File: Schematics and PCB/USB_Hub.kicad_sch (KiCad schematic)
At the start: 95 parts, among them J6 UPSTREAM, J7 DOWNSTREAM_3, J8 DOWNSTREAM_1, J9 DOWNSTREAM_2, U16 TUSB8042A, U17 TPS2561, U18 TLV71311PDBVR, U19 TLV70033DDCR, U20 TPS2561, Y1 24MHz 20pF GND24

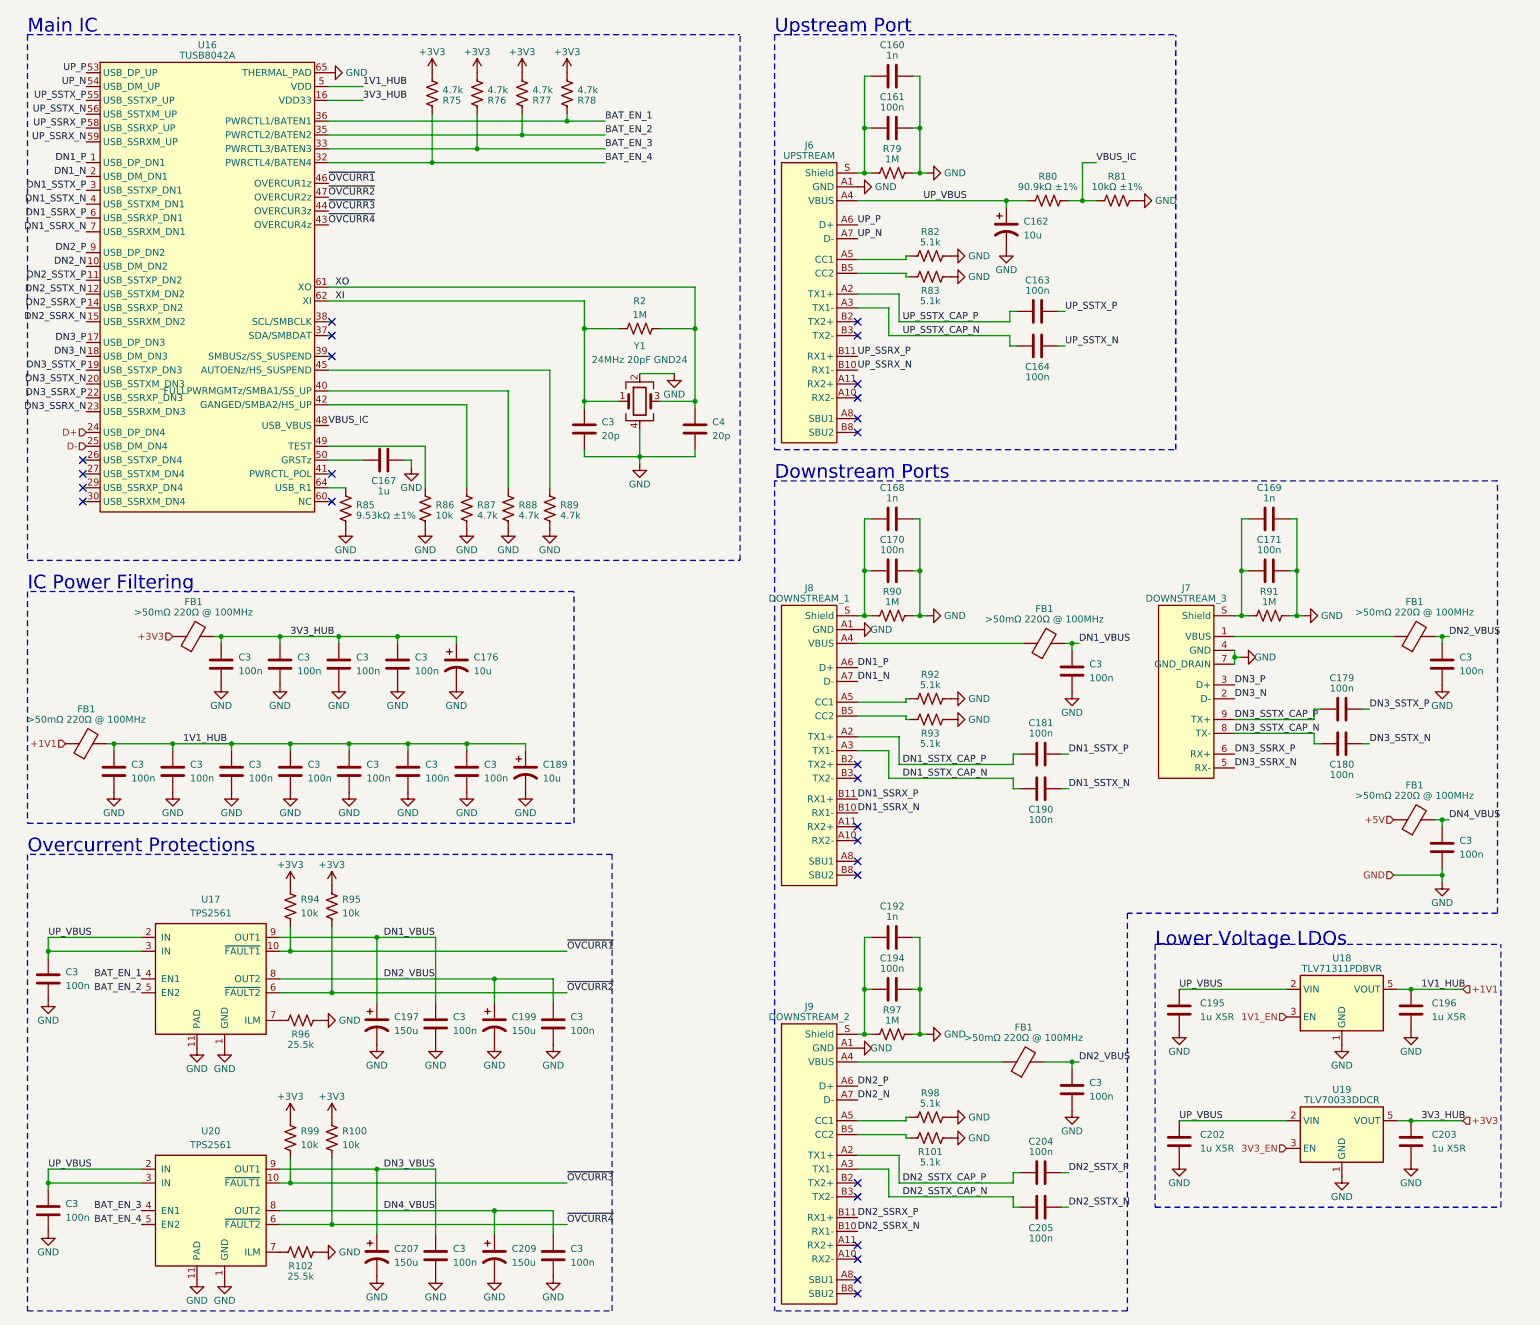
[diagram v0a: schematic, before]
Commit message: route most of the differential pairs
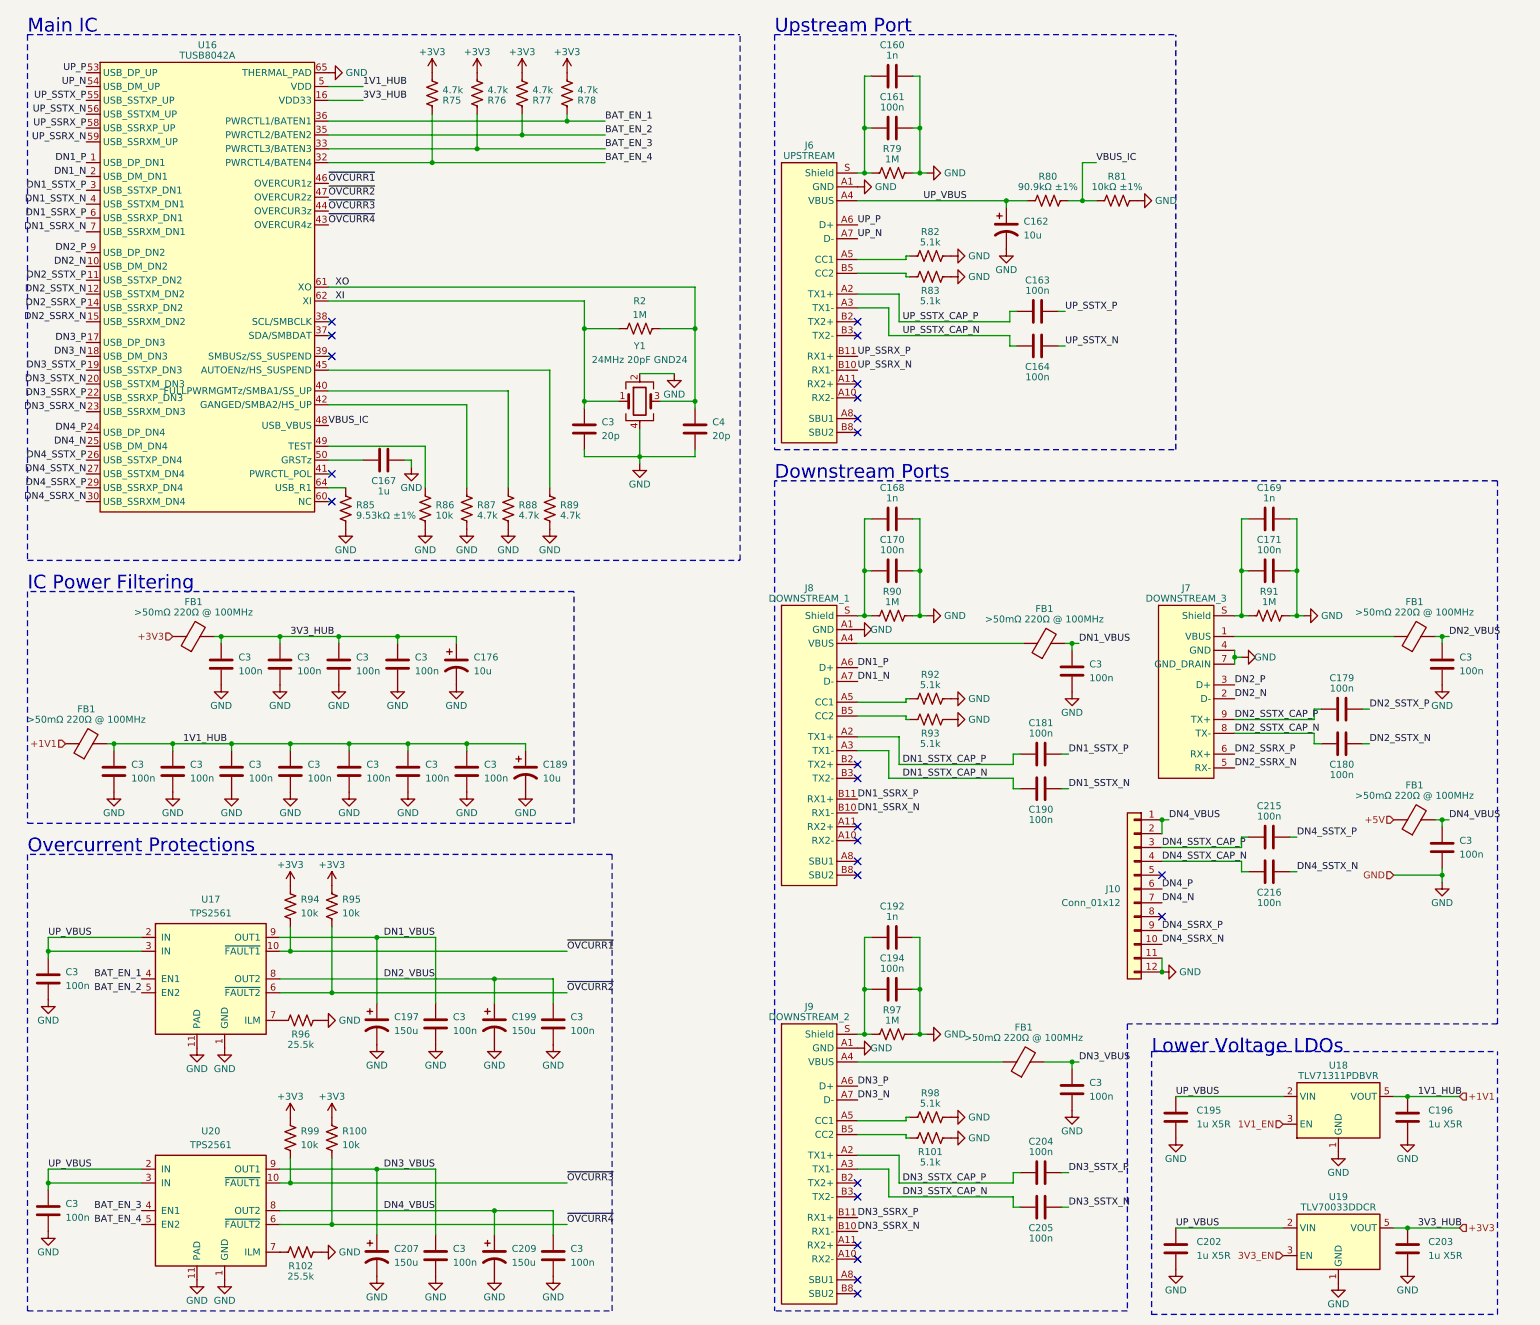
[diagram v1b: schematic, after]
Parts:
- added C215, C216: 100n, Capacitor_SMD:C_0603_1608Metric, symbol Device:C
- added J10: Conn_01x12, Connector_FFC-FPC:Hirose_FH12-12S-0.5SH_1x12-1MP_P0.50mm_Horizontal, symbol Connector_Generic:Conn_01x12
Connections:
- net DN2_N: now also J7.2 (D-); no longer J9.A7 (D-), J9.B7 (D-)
- net DN2_P: now also J7.3 (D+); no longer J9.A6 (D+), J9.B6 (D+)
- net DN2_SSRX_N: now also J7.5 (RX-); no longer J9.B10 (RX1-)
- net DN2_SSRX_P: now also J7.6 (RX+); no longer J9.B11 (RX1+)
- net DN2_SSTX_CAP_N: now also C180.1, J7.8 (TX-); no longer C205.1, J9.A3 (TX1-)
- net DN2_SSTX_CAP_P: now also C179.1, J7.9 (TX+); no longer C204.1, J9.A2 (TX1+)
- net DN2_SSTX_N: now also C180.2; no longer C205.2
- net DN2_SSTX_P: now also C179.2; no longer C204.2
- net DN2_VBUS: no longer C3.1, FB1.2
- net DN3_N: now also J9.A7 (D-), J9.B7 (D-); no longer J7.2 (D-)
- net DN3_P: now also J9.A6 (D+), J9.B6 (D+); no longer J7.3 (D+)
- net DN3_SSRX_N: now also J9.B10 (RX1-); no longer J7.5 (RX-)
- net DN3_SSRX_P: now also J9.B11 (RX1+); no longer J7.6 (RX+)
- net DN3_SSTX_CAP_N: now also C205.1, J9.A3 (TX1-); no longer C180.1, J7.8 (TX-)
- net DN3_SSTX_CAP_P: now also C204.1, J9.A2 (TX1+); no longer C179.1, J7.9 (TX+)
- net DN3_SSTX_N: now also C205.2; no longer C180.2
- net DN3_SSTX_P: now also C204.2; no longer C179.2
- net DN3_VBUS: now also C3.1, FB1.2
- net DN4_VBUS: now also J10.1 (Pin_1), J10.2 (Pin_2)
- net GND: now also J10.11 (Pin_11), J10.12 (Pin_12)
- net DN4_SSTX_P: now reaches U16.26 (USB_SSTXP_DN4)
- net DN4_SSTX_P: now also C215.2
- net DN4_SSTX_N: now reaches U16.27 (USB_SSTXM_DN4)
- net DN4_SSTX_N: now also C216.2
- net DN4_SSRX_P: now reaches U16.29 (USB_SSRXP_DN4)
- net DN4_SSRX_P: now also J10.9 (Pin_9)
- net DN4_SSRX_N: now reaches U16.30 (USB_SSRXM_DN4)
- net DN4_SSRX_N: now also J10.10 (Pin_10)
- net D+ renamed DN4_P
- net DN4_P: now also J10.6 (Pin_6)
- net D- renamed DN4_N
- net DN4_N: now also J10.7 (Pin_7)
- new net DN4_SSTX_CAP_N: C216.1, J10.4 (Pin_4)
- new net DN4_SSTX_CAP_P: C215.1, J10.3 (Pin_3)
- no-connect marks 27 -> 25
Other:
- moved on the sheet: C195, C196, C202, C203, U18, U19

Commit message: Differential pairs routed on the hub
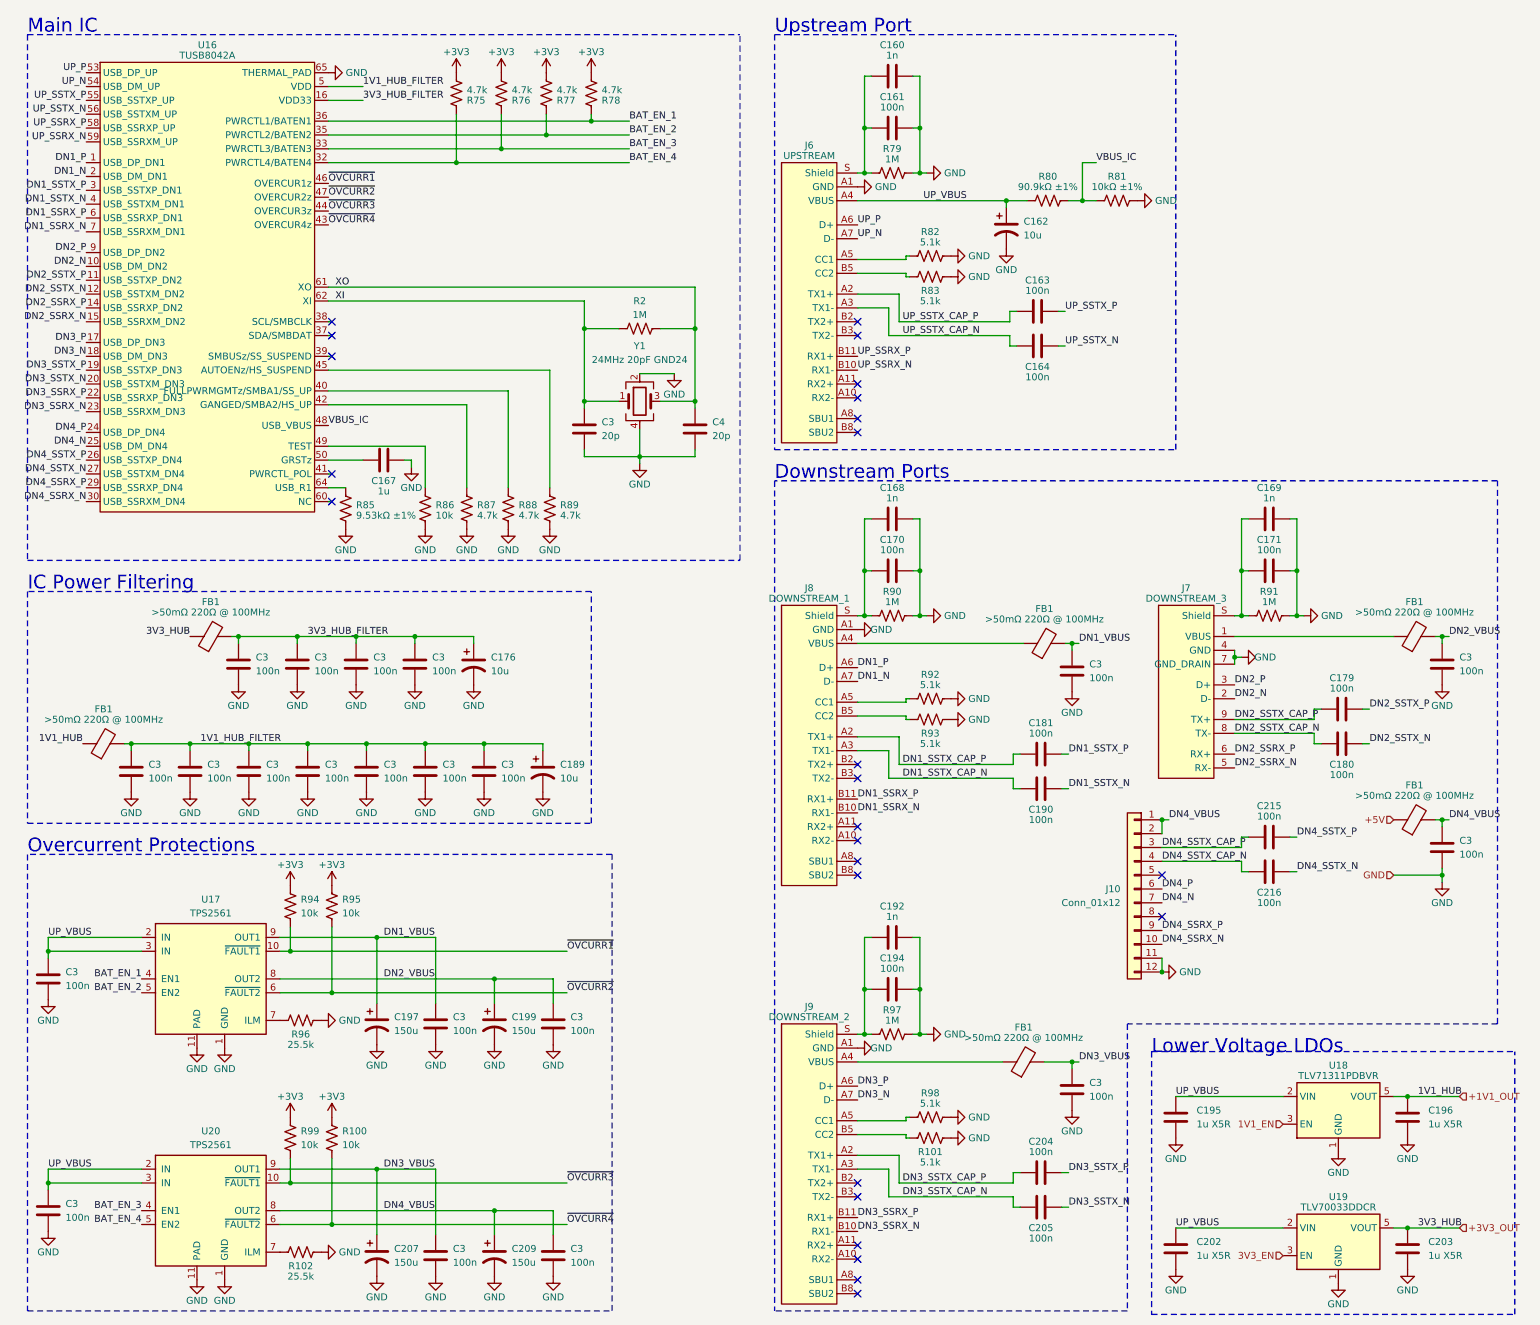
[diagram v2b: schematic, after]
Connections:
- net +3V3: no longer C176.1, C203.1, C3.1, C3.1, C3.1, C3.1, FB1.1, FB1.2, U16.16 (VDD33), U16.34 (VDD33), U16.52 (VDD33), U16.63 (VDD33), U19.5 (VOUT)
- net +1V1 renamed 1V1_HUB_FILTER
- net 1V1_HUB_FILTER: no longer C196.1, FB1.1, U18.5 (VOUT)
- new net +1V1_OUT: C196.1, FB1.1, U18.5 (VOUT)
- new net +3V3_OUT: C203.1, FB1.1, U19.5 (VOUT)
- new net 3V3_HUB_FILTER: C176.1, C3.1, C3.1, C3.1, C3.1, FB1.2, U16.16 (VDD33), U16.34 (VDD33), U16.52 (VDD33), U16.63 (VDD33)
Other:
- moved on the sheet: C176, C189, C3, FB1, R75, R76, R77, R78

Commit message: restarted hub layout
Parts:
- C162: footprint (none) -> Capacitor_Tantalum_SMD:CP_EIA-3216-18_Kemet-A
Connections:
- net 1V1_EN: now also J10.5 (Pin_5)
- net 3V3_EN: now also J10.6 (Pin_6)
- net DN4_N: now also J10.8 (Pin_8); no longer J10.7 (Pin_7)
- net DN4_P: now also J10.7 (Pin_7); no longer J10.6 (Pin_6)
- net DN4_VBUS: no longer J10.1 (Pin_1), J10.2 (Pin_2)
- net at C168.1, C170.1, R90.1: now also J8.S1 (Shield); no longer J8.S (Shield)
- net at C160.1, C161.1, R79.1: now also J6.S1 (Shield); no longer J6.S (Shield)
- net at C192.1, C194.1, R97.1: now also J9.S1 (Shield); no longer J9.S (Shield)
- net +5V renamed DN4_CONN
- net DN4_CONN: now also J10.1 (Pin_1), J10.2 (Pin_2)
- no-connect marks 25 -> 23
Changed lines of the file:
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@@
   (junction (at 81.28 182.88) (diameter 0) (color 0 0 0 0)
   )
-  (junction (at 276.86 171.45) (diameter 0) (color 0 0 0 0)
-  )
   (junction (at 210.82 47.625) (diameter 0) (color 0 0 0 0)
   )
@@
   (no_connect (at 169.545 227.965))
   (no_connect (at 169.545 153.67))
-  (no_connect (at 225.425 179.07))
   (no_connect (at 169.545 171.45))
   (no_connect (at 73.025 97.79))
-  (no_connect (at 225.425 171.45))
   (no_connect (at 169.545 168.91))
   (no_connect (at 169.545 245.745))
@@
     (stroke (width 0) (type default))
   )
+  (wire (pts (xy 266.7 161.29) (xy 267.97 161.29))
+    (stroke (width 0) (type default))
+  )
   (wire (pts (xy 104.14 38.1) (xy 127.635 38.1))
     (stroke (width 0) (type default))
@@
     (stroke (width 0) (type dash))
   )
-  (wire (pts (xy 276.86 171.45) (xy 276.86 172.72))
-    (stroke (width 0) (type default))
-  )
   (wire (pts (xy 68.58 147.32) (xy 79.375 147.32))
     (stroke (width 0) (type default))
@@
     (stroke (width 0) (type default))
   )
-  (wire (pts (xy 276.86 170.18) (xy 276.86 171.45))
-    (stroke (width 0) (type default))
-  )
   (wire (pts (xy 81.28 182.88) (xy 63.5 182.88))
     (stroke (width 0) (type default))
@@
     (stroke (width 0) (type default))
   )
-  (wire (pts (xy 267.97 171.45) (xy 276.86 171.45))
-    (stroke (width 0) (type default))
-  )
   (wire (pts (xy 225.425 168.91) (xy 240.03 168.91))
     (stroke (width 0) (type default))
@@
     (effects (font (size 1.27 1.27)) (justify left bottom))
   )
-  (label "DN4_VBUS" (at 226.695 161.29 0) (fields_autoplaced)
+  (label "DN4_P" (at 225.425 176.53 0) (fields_autoplaced)
+    (effects (font (size 1.27 1.27)) (justify left bottom))
+  )
+  (label "DN4_CONN" (at 226.695 161.29 0) (fields_autoplaced)
     (effects (font (size 1.27 1.27)) (justify left bottom))
   )
@@
     (effects (font (size 1.27 1.27)) (justify left bottom))
   )
+  (label "DN4_CONN" (at 266.7 161.29 180) (fields_autoplaced)
+    (effects (font (size 1.27 1.27)) (justify right bottom))
+  )
   (label "DN1_N" (at 27.94 43.18 180) (fields_autoplaced)
     (effects (font (size 1.27 1.27)) (justify right bottom))
@@
     (effects (font (size 1.27 1.27)) (justify right bottom))
   )
+  (label "1V1_EN" (at 247.65 217.17 180) (fields_autoplaced)
+    (effects (font (size 1.27 1.27)) (justify right bottom))
+  )
   (label "DN2_SSTX_N" (at 27.94 64.77 180) (fields_autoplaced)
     (effects (font (size 1.27 1.27)) (justify right bottom))
@@
     (effects (font (size 1.27 1.27)) (justify left bottom))
   )
+  (label "1V1_EN" (at 225.425 171.45 0) (fields_autoplaced)
+    (effects (font (size 1.27 1.27)) (justify left bottom))
+  )
   (label "1V1_HUB" (at 272.415 212.09 0) (fields_autoplaced)
     (effects (font (size 1.27 1.27)) (justify left bottom))
@@
     (effects (font (size 1.27 1.27)) (justify right bottom))
   )
-  (label "DN4_N" (at 225.425 176.53 0) (fields_autoplaced)
-    (effects (font (size 1.27 1.27)) (justify left bottom))
-  )
   (label "UP_SSTX_P" (at 27.94 29.21 180) (fields_autoplaced)
     (effects (font (size 1.27 1.27)) (justify right bottom))
   )
+  (label "3V3_EN" (at 247.65 241.3 180) (fields_autoplaced)
+    (effects (font (size 1.27 1.27)) (justify right bottom))
+  )
+  (label "3V3_EN" (at 225.425 173.99 0) (fields_autoplaced)
+    (effects (font (size 1.27 1.27)) (justify left bottom))
+  )
   (label "DN3_N" (at 169.545 212.725 0) (fields_autoplaced)
     (effects (font (size 1.27 1.27)) (justify left bottom))
@@
     (effects (font (size 1.27 1.27)) (justify left bottom))
   )
+  (label "DN4_N" (at 225.425 179.07 0) (fields_autoplaced)
+    (effects (font (size 1.27 1.27)) (justify left bottom))
+  )
   (label "~{OVCURR2}" (at 116.205 193.04 0) (fields_autoplaced)
     (effects (font (size 1.27 1.27)) (justify left bottom))
@@
     (effects (font (size 1.27 1.27)) (justify right bottom))
   )
-  (label "DN4_P" (at 225.425 173.99 0) (fields_autoplaced)
-    (effects (font (size 1.27 1.27)) (justify left bottom))
-  )
   (label "BAT_EN_3" (at 127.635 38.1 0) (fields_autoplaced)
     (effects (font (size 1.27 1.27)) (justify left bottom))
@@
     (effects (font (size 1.27 1.27)) (justify left))
   )
-  (hierarchical_label "GND" (shape input) (at 267.97 171.45 180) (fields_autoplaced)
-    (effects (font (size 1.27 1.27)) (justify right))
-  )
   (hierarchical_label "+3V3_OUT" (shape input) (at 280.035 236.22 0) (fields_autoplaced)
     (effects (font (size 1.27 1.27)) (justify left))
   )
-  (hierarchical_label "1V1_EN" (shape input) (at 247.65 217.17 180) (fields_autoplaced)
-    (effects (font (size 1.27 1.27)) (justify right))
-  )
-  (hierarchical_label "3V3_EN" (shape input) (at 247.65 241.3 180) (fields_autoplaced)
-    (effects (font (size 1.27 1.27)) (justify right))
-  )
-  (hierarchical_label "+5V" (shape input) (at 267.97 161.29 180) (fields_autoplaced)
-    (effects (font (size 1.27 1.27)) (justify right))
-  )
   (symbol (lib_id "Device:R_US") (at 75.565 104.14 0) (unit 1)
     (in_bom yes) (on_board yes) (dnp no)
@@
     (pin "B8")
     (pin "B9")
-    (pin "S")
+    (pin "S1")
     (instances
       (project "Schematics and PCB"
@@
       (effects (font (size 1.27 1.27)) (justify left))
     )
-    (property "Footprint" "" (at 196.85 52.705 0)
+    (property "Footprint" "Capacitor_Tantalum_SMD:CP_EIA-3216-18_Kemet-A" (at 196.85 52.705 0)
       (effects (font (size 1.27 1.27)) hide)
     )
@@
     (pin "B8")
     (pin "B9")
-    (pin "S")
+    (pin "S1")
     (instances
       (project "Schematics and PCB"
@@
     (pin "B8")
     (pin "B9")
-    (pin "S")
+    (pin "S1")
     (instances
       (project "Schematics and PCB"
@@
     )
   )
-  (symbol (lib_id "power:GND") (at 276.86 172.72 0) (unit 1)
+  (symbol (lib_id "power:GND") (at 276.86 170.18 0) (unit 1)
     (in_bom yes) (on_board yes) (dnp no)
-    (property "Reference" "#PWR07" (at 276.86 179.07 0)
+    (property "Reference" "#PWR07" (at 276.86 176.53 0)
       (effects (font (size 1.27 1.27)) hide)
     )
-    (property "Value" "GND" (at 276.86 176.53 0)
+    (property "Value" "GND" (at 276.86 173.99 0)
       (effects (font (size 1.27 1.27)))
     )
-    (property "Footprint" "" (at 276.86 172.72 0)
+    (property "Footprint" "" (at 276.86 170.18 0)
       (effects (font (size 1.27 1.27)) hide)
     )
-    (property "Datasheet" "" (at 276.86 172.72 0)
+    (property "Datasheet" "" (at 276.86 170.18 0)
       (effects (font (size 1.27 1.27)) hide)
     )
